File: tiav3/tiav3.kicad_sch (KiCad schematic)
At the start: 21 parts, among them J1 SSQ-103-01-G-D, J2 Conn_Coaxial, U1 OPA847IDBVT

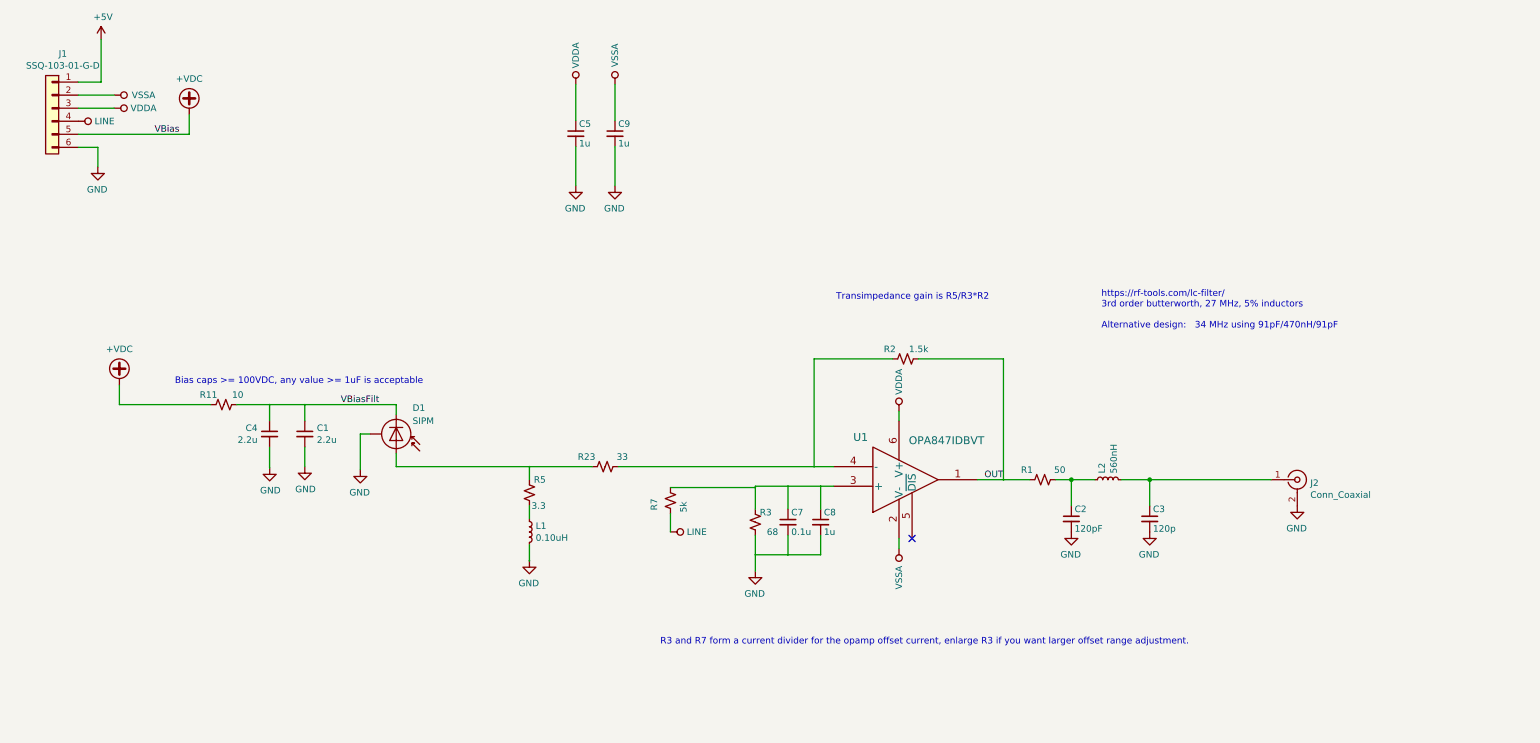
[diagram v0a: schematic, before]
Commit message: Add PZC for S14420-3050 to schematic
No functional changes, just adds the correct PZC filter values as a comment.
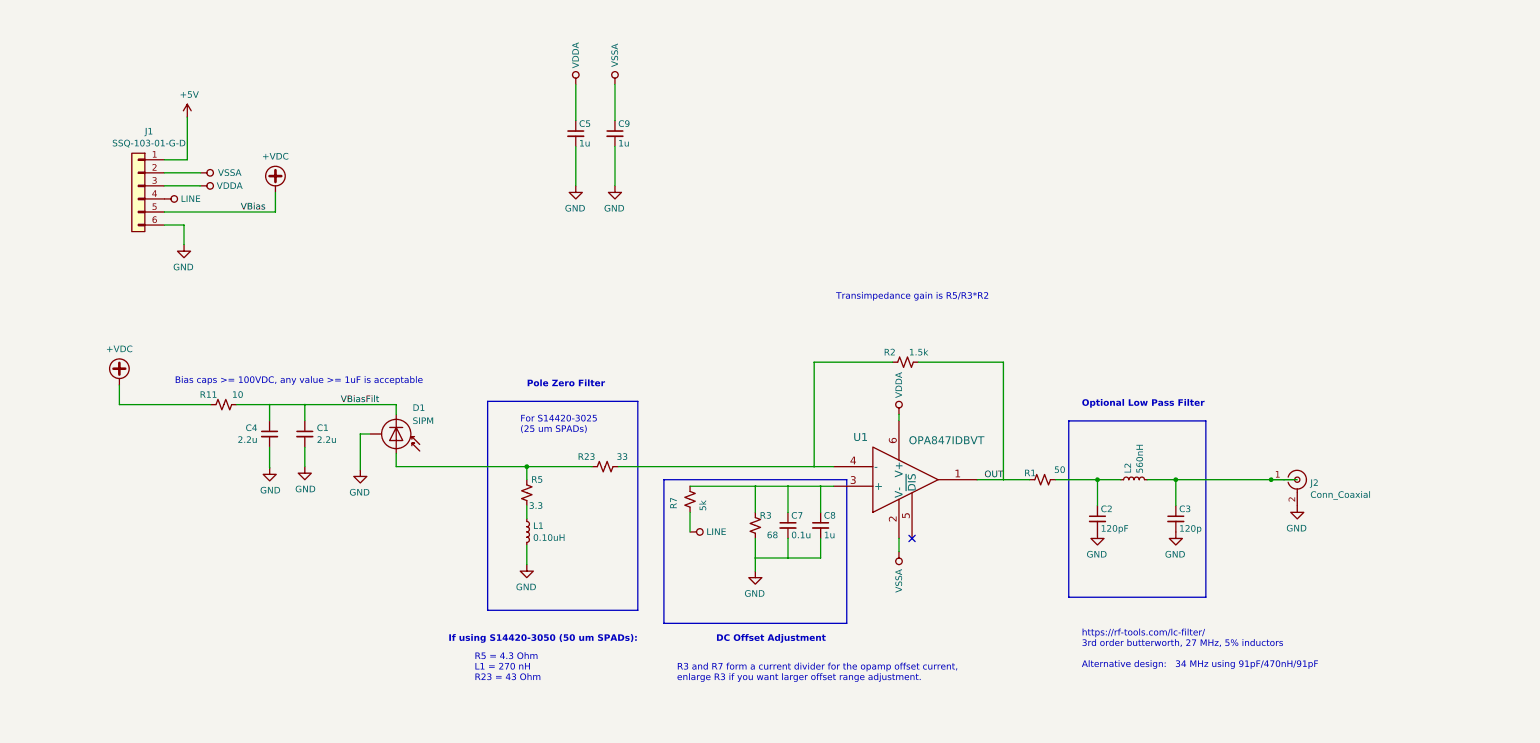
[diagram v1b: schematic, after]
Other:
- note added: "DC Offset Adjustment"
- note added: "For S14420-3025 (25 um SPADs)"
- note added: "If using S14420-3050 (50 um SPADs):"
- note added: "Optional Low Pass Filter"
- note added: "Pole Zero Filter"
- note added: "R5 = 4.3 Ohm L1 = 270 nH R23 = 43 Ohm"
- moved on the sheet: C2, C3, C7, C8, J1, L1, L2, R2, R3, R5, R7

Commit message: Improve low pass filter documentation and change default cut off
The 27 MHz default was a bit high since most objectives would not need this when paired with a 16 or 24 KHz scanner.

Adjust some of the footprints and text.

Bump to V11 to reflect the changed default LPF values.
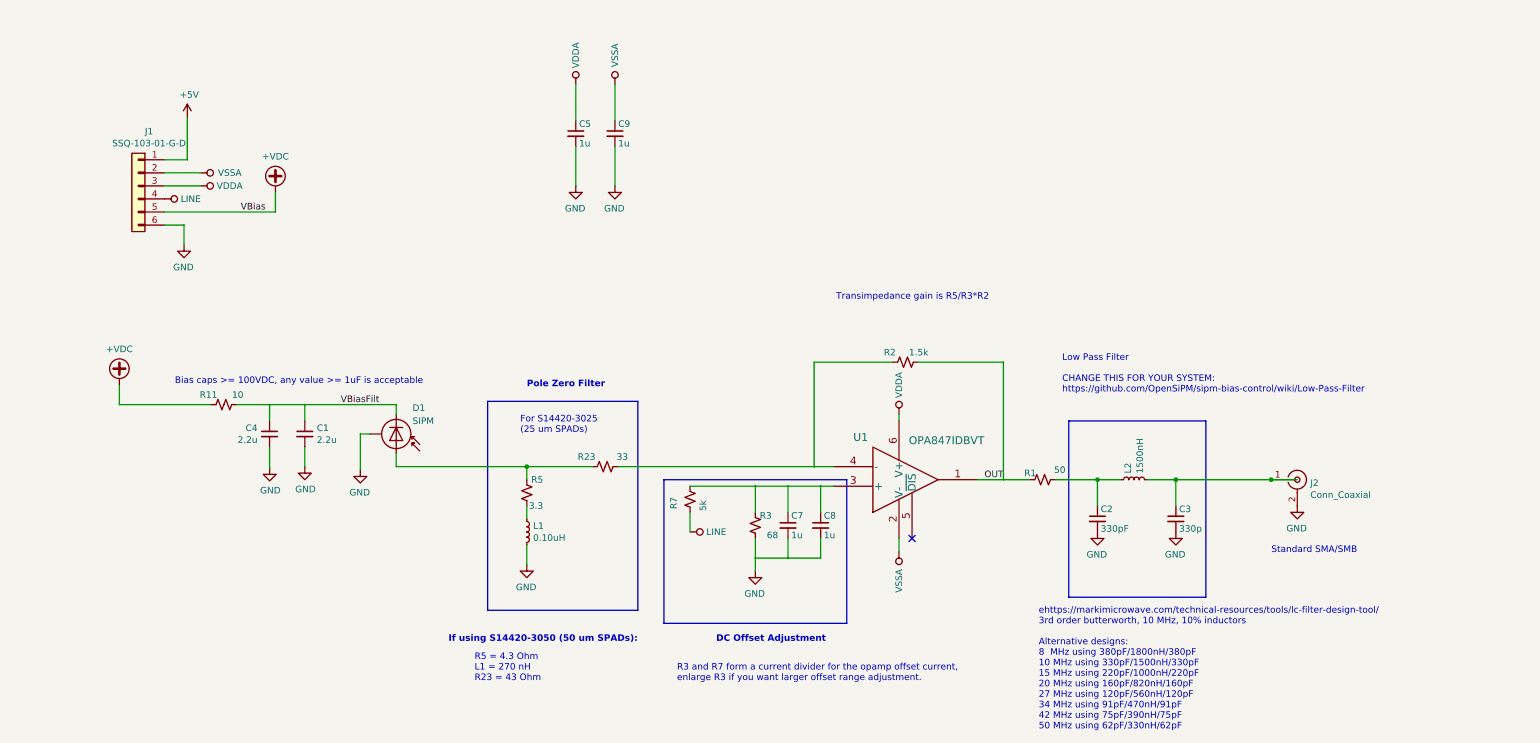
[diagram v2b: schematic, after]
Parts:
- C2: value 120pF -> 330pF
- C3: value 120p -> 330p
- C7: value 0.1u -> 1u
- L1: footprint footprints:L_0603_1608Metric -> Inductor_SMD:L_0603_1608Metric_Pad1.05x0.95mm_HandSolder
- L2: value 560nH -> 1500nH
- R1, R11, R2, R23, R3, R5, R7: footprint footprints:R_0402_1005Metric -> Resistor_SMD:R_0402_1005Metric_Pad0.72x0.64mm_HandSolder
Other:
- note added: "Low Pass Filter CHANGE THIS FOR YOUR SYSTEM: https://github.com/OpenSiPM/sipm-bias-control/wiki/Low-Pass-Filter"
- note added: "Standard SMA/SMB"
- note added: "ehttps://markimicrowave.com/technical-resources/tools/lc-filter-design-tool/ 3rd order butterworth, 10 MHz, 10% inductors Alternative designs: 8 MHz using 380pF/1800nH/380pF 10 MHz using 330pF/1500nH/330pF 15 MHz using 220pF/1000nH/220pF 20 MHz using 160pF/820nH/160pF 27 MHz using 120pF/560nH/120pF 34 MHz using 91pF/470nH/91pF 42 MHz using 75pF/390nH/75pF 50 MHz using 62pF/330nH/62pF"
- note removed: "Optional Low Pass Filter"
- note removed: "https://rf-tools.com/lc-filter/ 3rd order butterworth, 27 MHz, 5% inductors Alternative design: 34 MHz using 91pF/470nH/91pF"

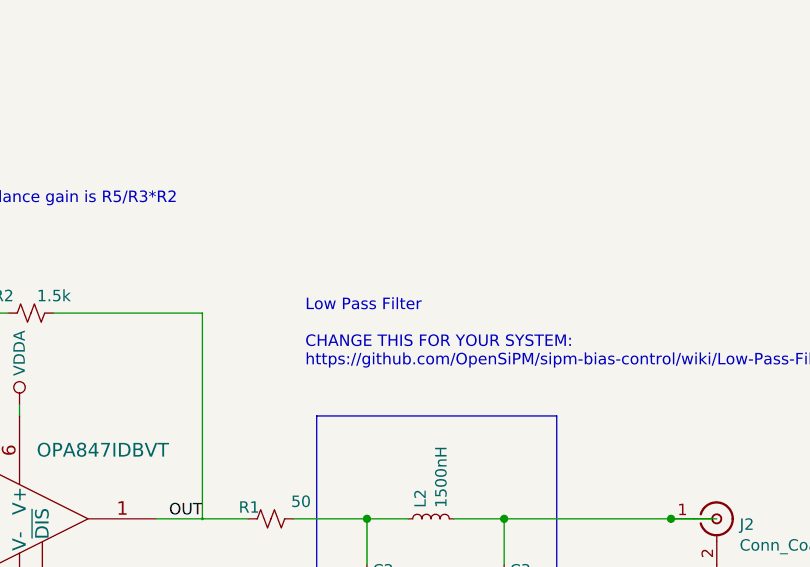
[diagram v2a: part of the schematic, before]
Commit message: Delete unneeded footprints
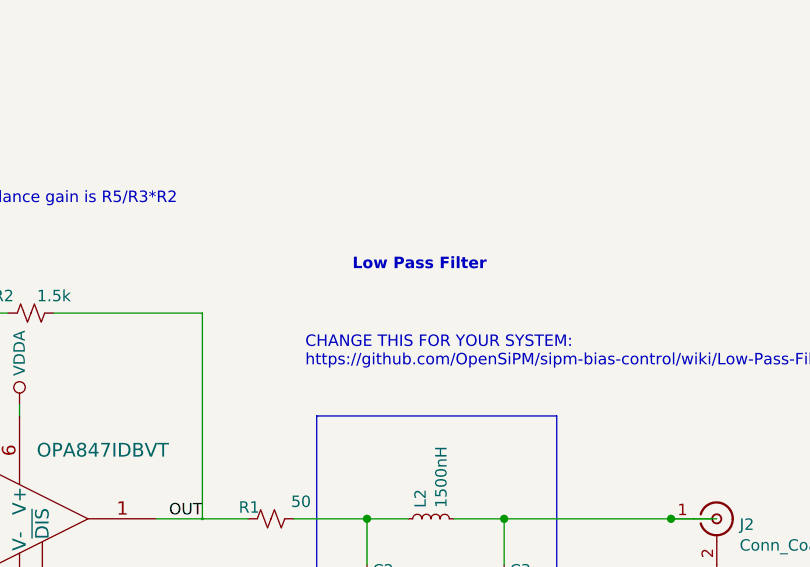
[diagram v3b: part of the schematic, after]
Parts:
- C8: footprint footprints:C_0402_1005Metric -> Capacitor_SMD:C_0402_1005Metric
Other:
- note added: "CHANGE THIS FOR YOUR SYSTEM: https://github.com/OpenSiPM/sipm-bias-control/wiki/Low-Pass-Filter"
- note added: "Low Pass Filter"
- note removed: "Low Pass Filter CHANGE THIS FOR YOUR SYSTEM: https://github.com/OpenSiPM/sipm-bias-control/wiki/Low-Pass-Filter"
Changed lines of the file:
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@@
 		)
 	)
-	(text "Low Pass Filter\n\nCHANGE THIS FOR YOUR SYSTEM:\nhttps://github.com/OpenSiPM/sipm-bias-control/wiki/Low-Pass-Filter"
+	(text "Low Pass Filter"
+		(exclude_from_sim no)
+		(at 231.14 82.296 0)
+		(effects
+			(font
+				(size 1.27 1.27)
+				(thickness 0.254)
+				(bold yes)
+			)
+		)
+	)
+	(text "CHANGE THIS FOR YOUR SYSTEM:\nhttps://github.com/OpenSiPM/sipm-bias-control/wiki/Low-Pass-Filter"
 		(exclude_from_sim no)
 		(at 218.44 93.726 0)
@@
 			)
 		)
-		(property "Footprint" "footprints:C_0402_1005Metric"
+		(property "Footprint" "Capacitor_SMD:C_0402_1005Metric"
 			(at 171.45 119.38 0)
 			(effects
